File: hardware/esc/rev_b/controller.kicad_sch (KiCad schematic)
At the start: 47 parts, among them J201 ESC_SWD, U201 RP2354B, U204 TPS3430WDRCR, U205 SN74LVC1G08DBVR, U206 TCAN3413DR, U207 MCP2518FD-H/QBB, Y201 12MHz ABM8-272-T3, Y202 40MHz ABM8G

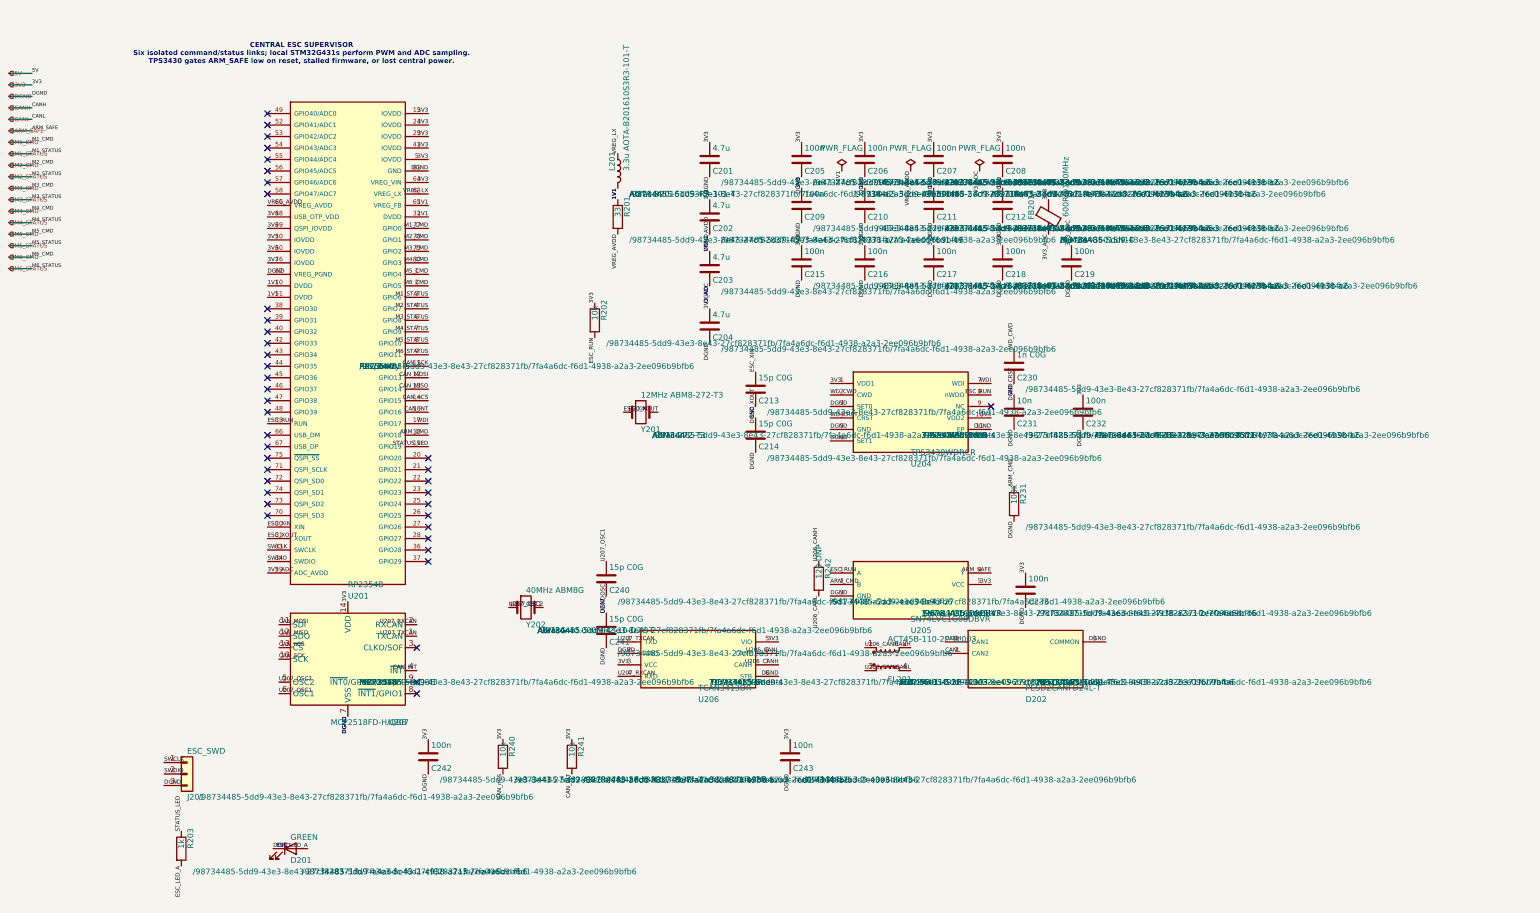
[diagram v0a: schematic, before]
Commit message: build: route and validate rev-b boards
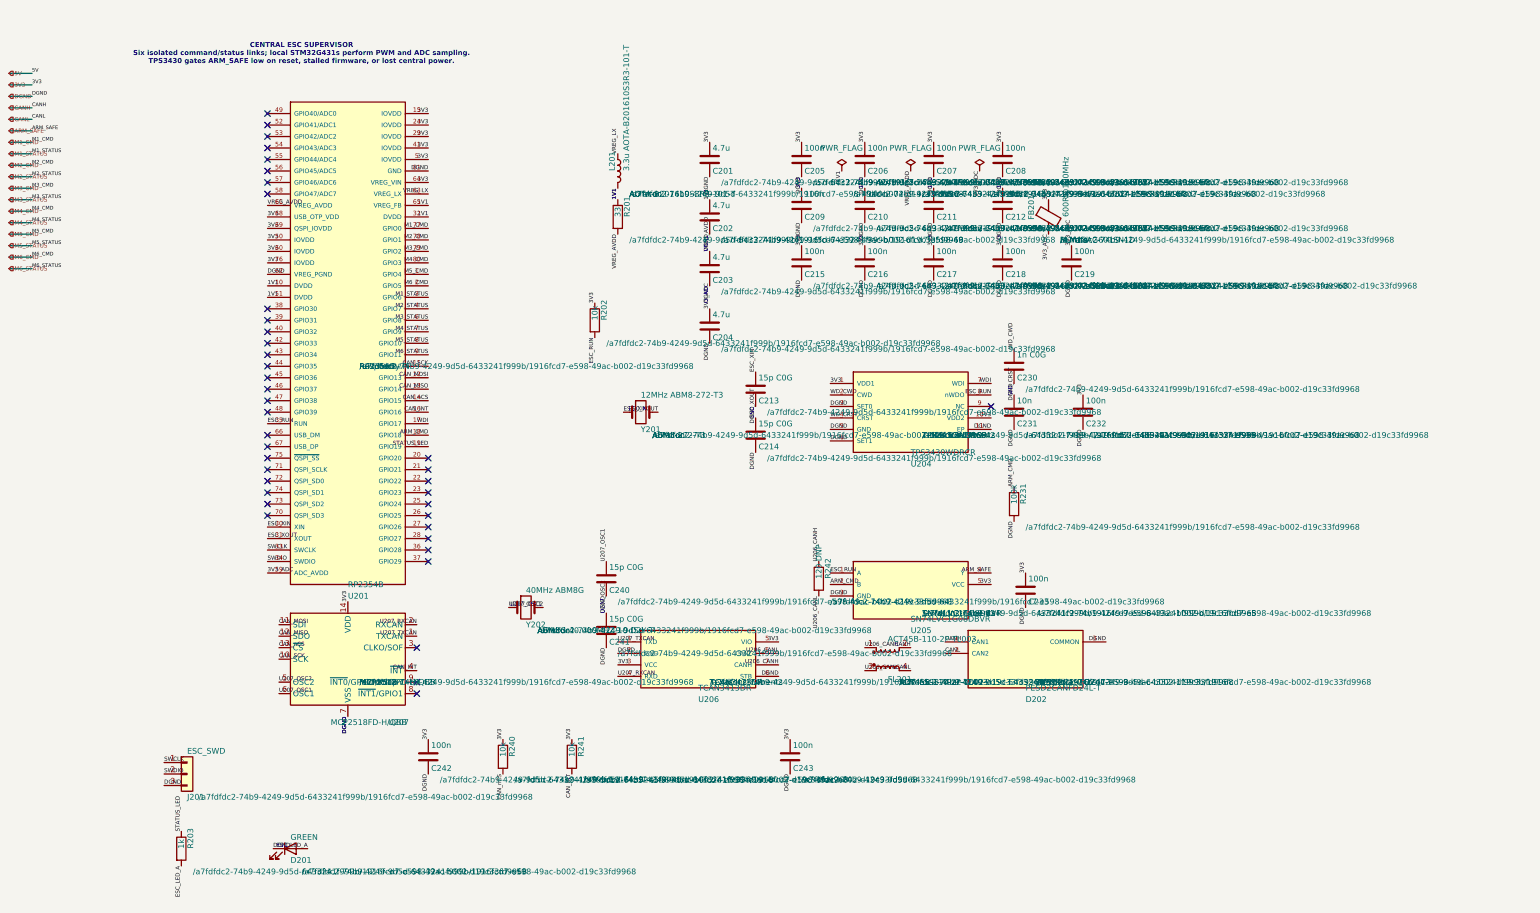
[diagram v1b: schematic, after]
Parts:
- C201, C202, C203, C204, C205, C206, C207, C208, C209, C210, C211, C212, C213, C214, C215, C216, C217, C218, C219, C230, C231, C232, C233, C240, C241, C242, C243, D201, D202, FB201, J201, L201, R201, R202, R203, R231, R240, R241, R242, U201, U204, U205, U206, U207, Y201, Y202: hierarchy_path /98734485-5dd9-43e3-8e43-27cf828371fb/7fa4a6dc-f6d1-4938-a2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 -> /a7fdfdc2-74b9-4249-9d5d-6433241f999b/1916fcd7-e598-49ac-b0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
- FL201: footprint Inductor_SMD:L_CommonModeChoke_Coilank_ACM4532 -> Inductor_SMD:L_CommonModeChoke_Coilcraft_1812CAN; hierarchy_path /98734485-5dd9-43e3-8e43-27cf828371fb/7fa4a6dc-f6d1-4938-a2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 -> /a7fdfdc2-74b9-4249-9d5d-6433241f999b/1916fcd7-e598-49ac-b0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

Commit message: build: route and validate rev-b boards
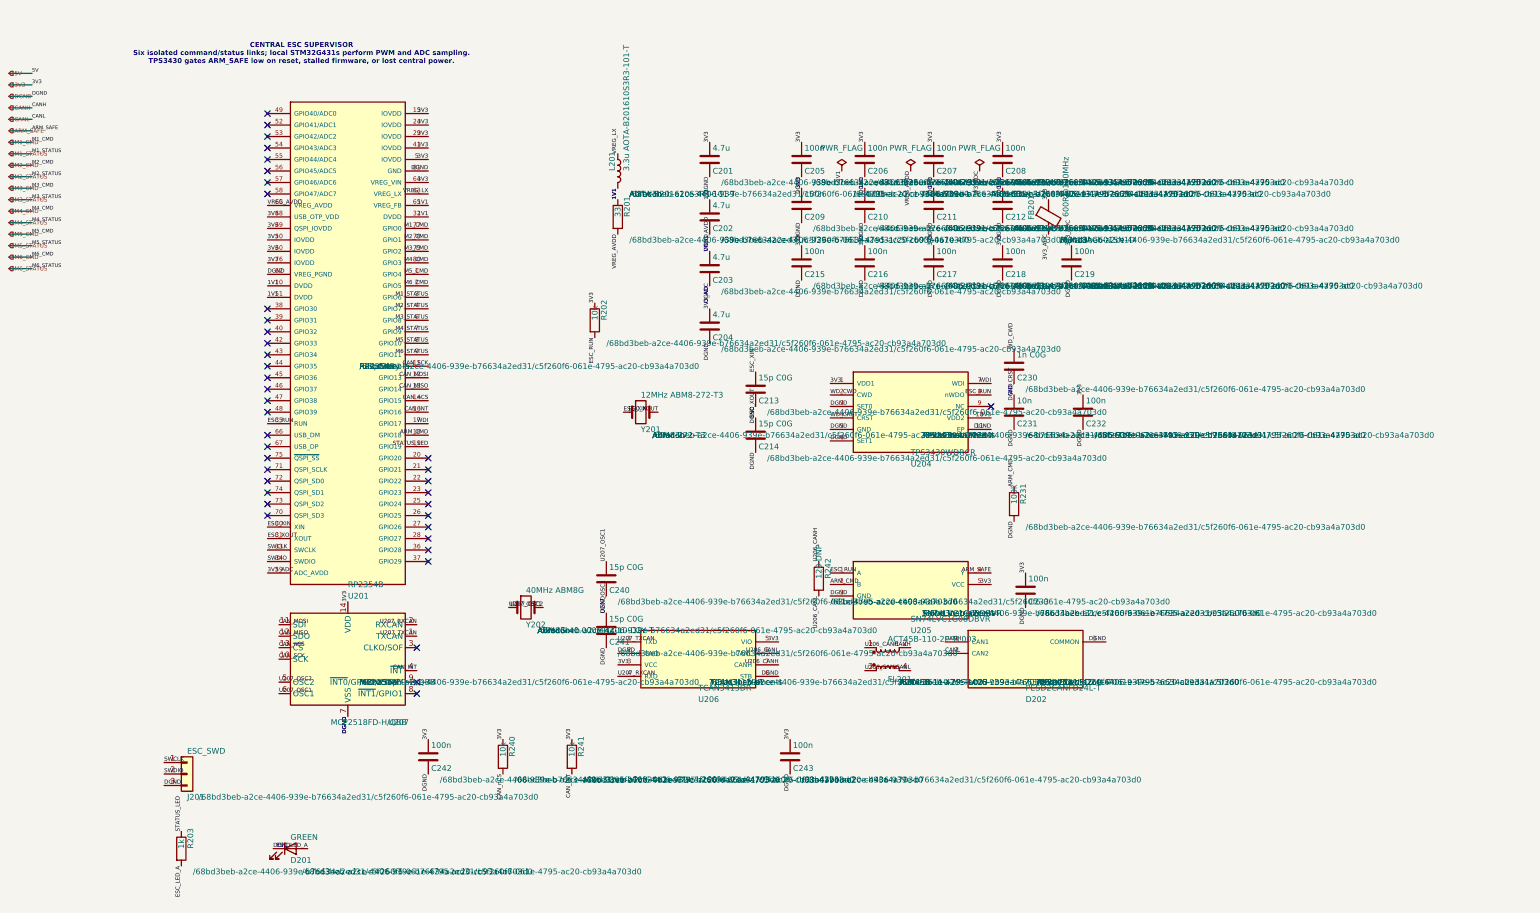
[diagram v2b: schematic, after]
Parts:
- C201, C202, C203, C204, C205, C206, C207, C208, C209, C210, C211, C212, C213, C214, C215, C216, C217, C218, C219, C230, C231, C232, C233, C240, C241, C242, C243, D201, D202, FB201, FL201, J201, L201, R201, R202, R203, R231, R240, R241, R242, U201, U204, U205, U206, U207, Y201, Y202: hierarchy_path /a7fdfdc2-74b9-4249-9d5d-6433241f999b/1916fcd7-e598-49ac-b0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 -> /68bd3beb-a2ce-4406-939e-b76634a2ed31/c5f260f6-061e-4795-ac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

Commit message: build: route and validate rev-b boards
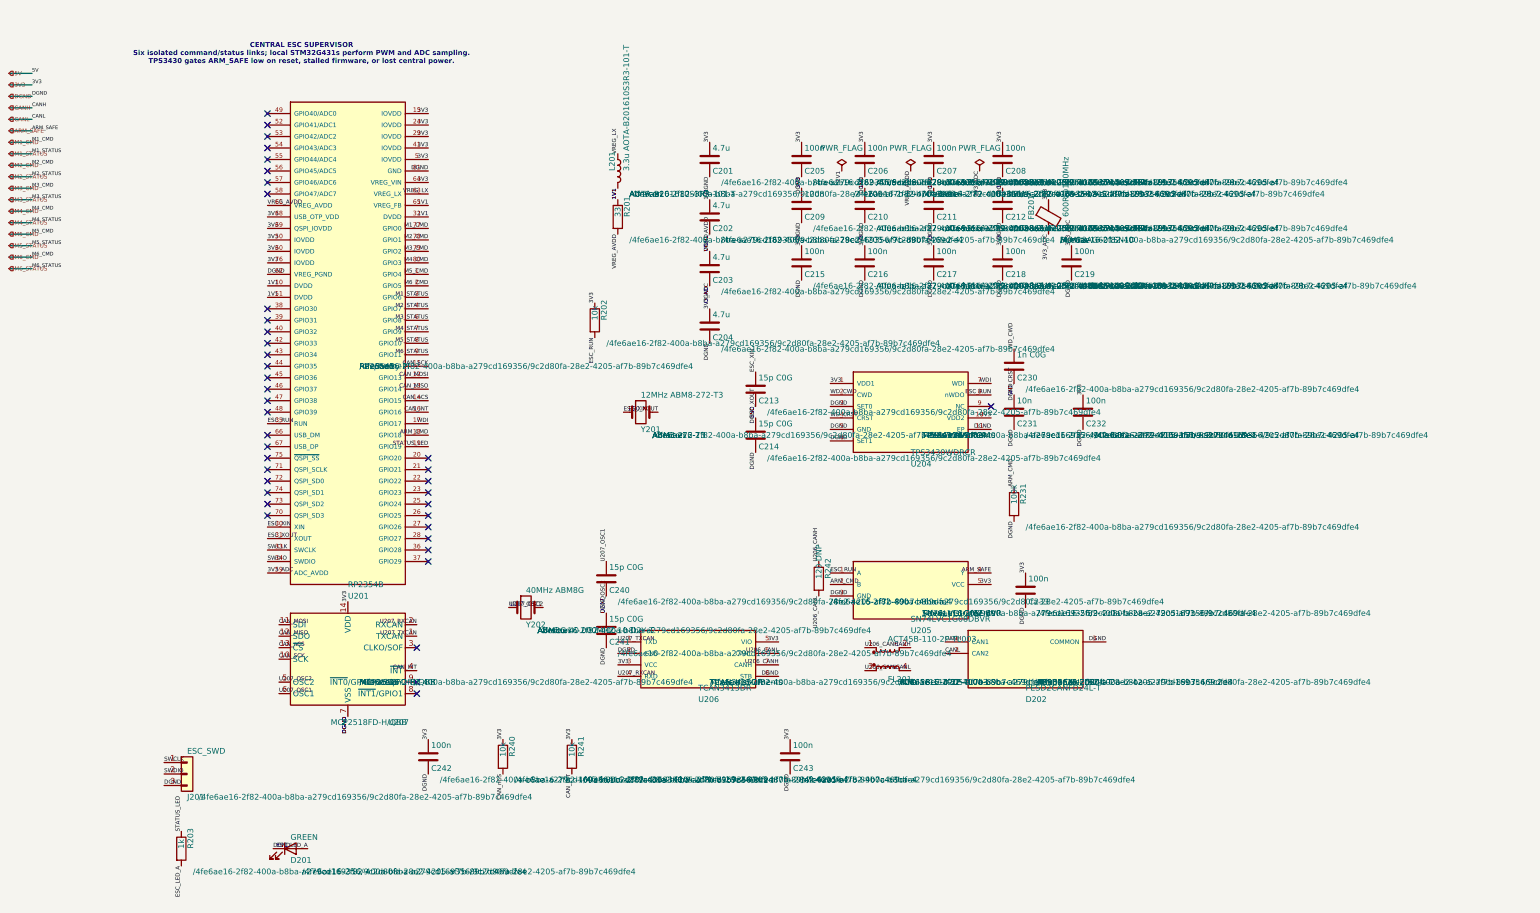
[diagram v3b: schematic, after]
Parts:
- C201, C202, C203, C204, C205, C206, C207, C208, C209, C210, C211, C212, C213, C214, C215, C216, C217, C218, C219, C230, C231, C232, C233, C240, C241, C242, C243, D201, D202, FB201, FL201, J201, L201, R201, R202, R203, R231, R240, R241, R242, U201, U204, U205, U206, U207, Y201, Y202: hierarchy_path /68bd3beb-a2ce-4406-939e-b76634a2ed31/c5f260f6-061e-4795-ac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 -> /4fe6ae16-2f82-400a-b8ba-a279cd169356/9c2d80fa-28e2-4205-af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
